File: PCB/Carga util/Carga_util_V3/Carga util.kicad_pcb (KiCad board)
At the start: 2 copper layers, 50 x 48.5 mm, 42 parts, among them J1 UART, J2 CONN, J3 DEBUG, J4 BG51, Q1 NMOS, Q2 NMOS, SW1 Reset, U1 LM1117DT-3.3, U2 ATtiny85-20S

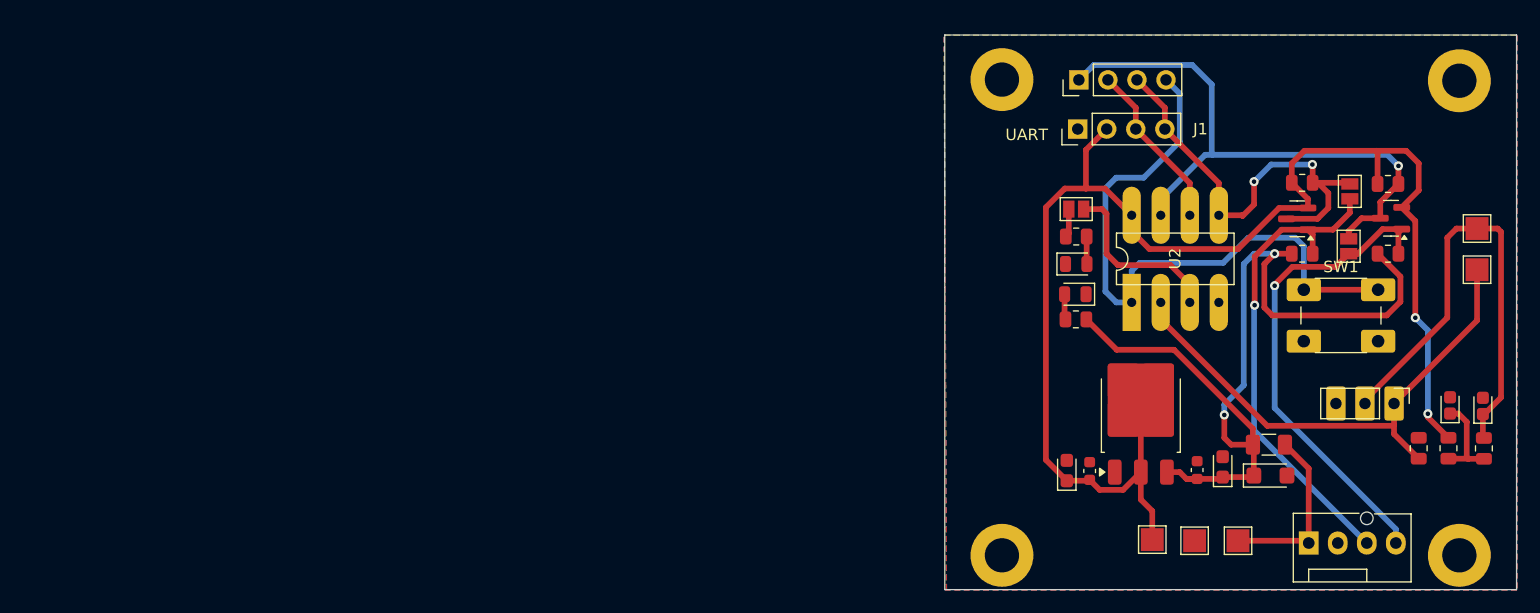
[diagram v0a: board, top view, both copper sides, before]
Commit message: update pcb para pocket
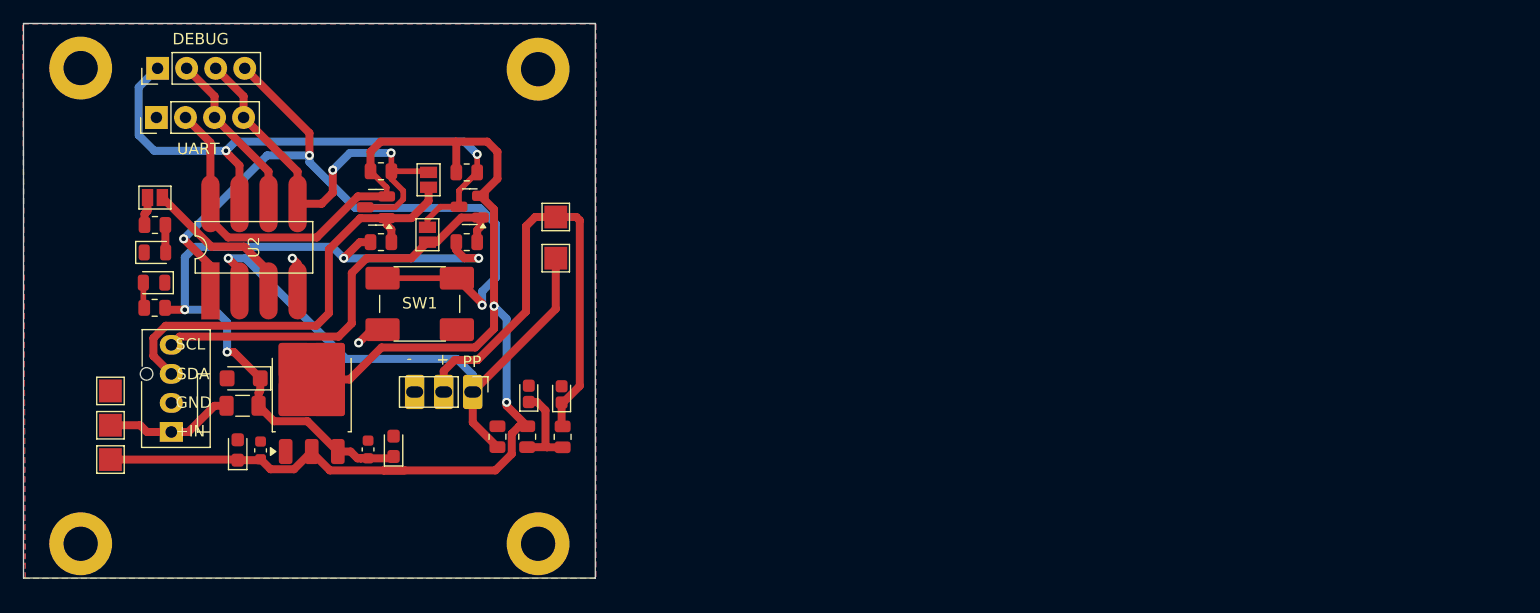
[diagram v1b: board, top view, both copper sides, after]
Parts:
- moved J2 99.9 mm to (132.3, 98.7), turned to 90 degrees
- moved IN 99.1 mm to (127.0, 98.1)
- moved GND 95.7 mm to (127.0, 95.1)
- moved +3.3V 91.4 mm to (127.0, 101.1)
- moved D1 90.2 mm to (138.7, 94.0), turned to 180 degrees
- moved F1 89.8 mm to (138.6, 96.4), turned to 180 degrees
- moved ? 80.6 mm to (124.4, 66.9)
- moved C5 80.6 mm to (163.6, 95.4)
- moved C6 80.6 mm to (166.4, 95.4)
- moved D2 80.6 mm to (130.8, 85.6)
- moved D3 80.6 mm to (130.9, 83.0)
- moved J1 80.6 mm to (131.0, 71.2)
- moved J3 80.6 mm to (131.1, 66.9)
- moved J4 80.6 mm to (158.7, 95.2)
- moved JP1 80.6 mm to (130.9, 78.2)
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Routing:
- net +3.7V: track 76.6 -> 65.7 mm, vias 2 -> 4
- net /SS: track 55.4 -> 66.0 mm, vias 0 -> 3
- net +3.3V: track 124.8 -> 135.2 mm
- net GND: track 0.00 -> 6.64 mm, vias 0 -> 2
- net /SCL_HV: track 42.7 -> 36.5 mm, vias 1 -> 0
- net /PP: track 46.2 -> 52.3 mm, vias 0 -> 1
- net /IN: track 15.7 -> 11.3 mm
- net /SDA_HV: track 42.6 -> 39.5 mm, vias 1 -> 0
- net Net-(JP1-B): track 15.6 -> 13.7 mm
- net /VDC_Filter: track 41.4 -> 42.6 mm
- net /SCK: track 52.4 -> 51.8 mm, vias 1 -> 2
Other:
- board text added: "+"
- board text added: "+IN"
- board text added: "-"
- board text added: "GND"
- board text added: "PP"
- board text added: "SCL"
- board text added: "SDA"

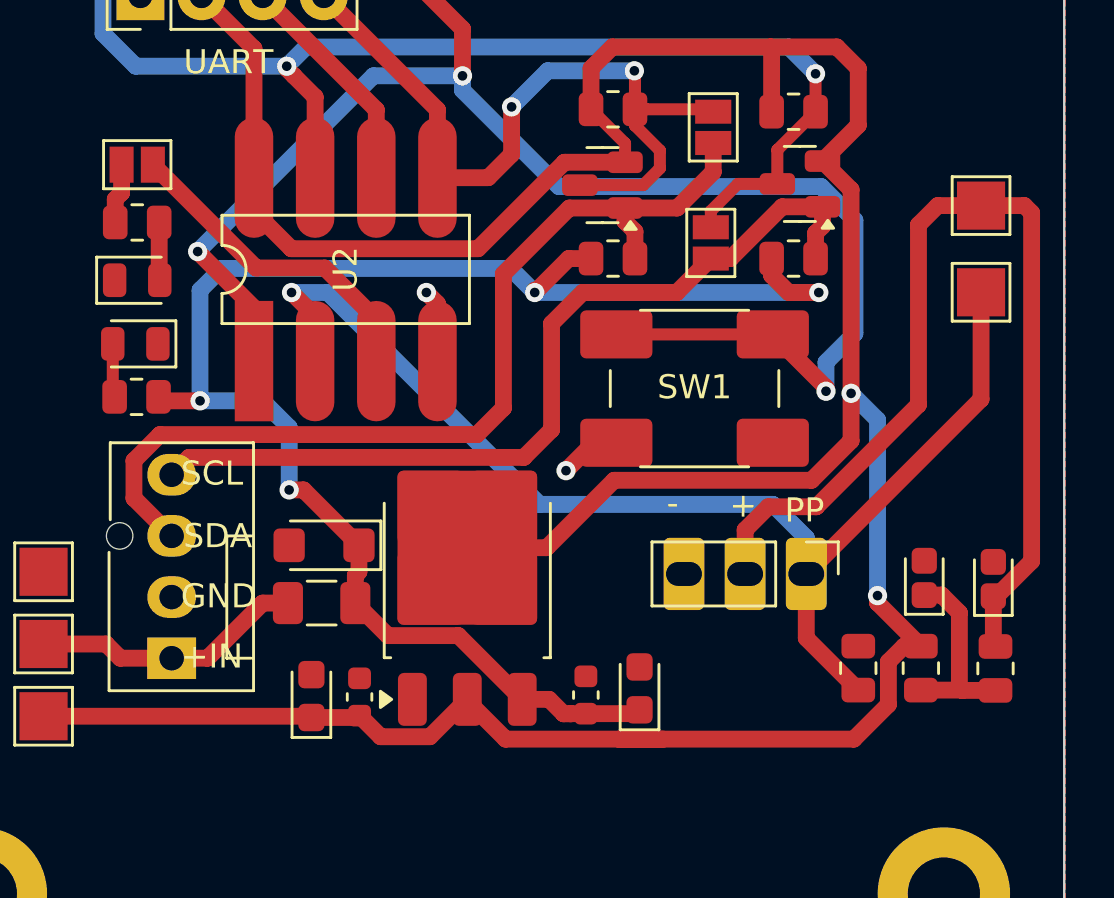
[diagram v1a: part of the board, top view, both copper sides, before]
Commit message: update 2 pcb pocket
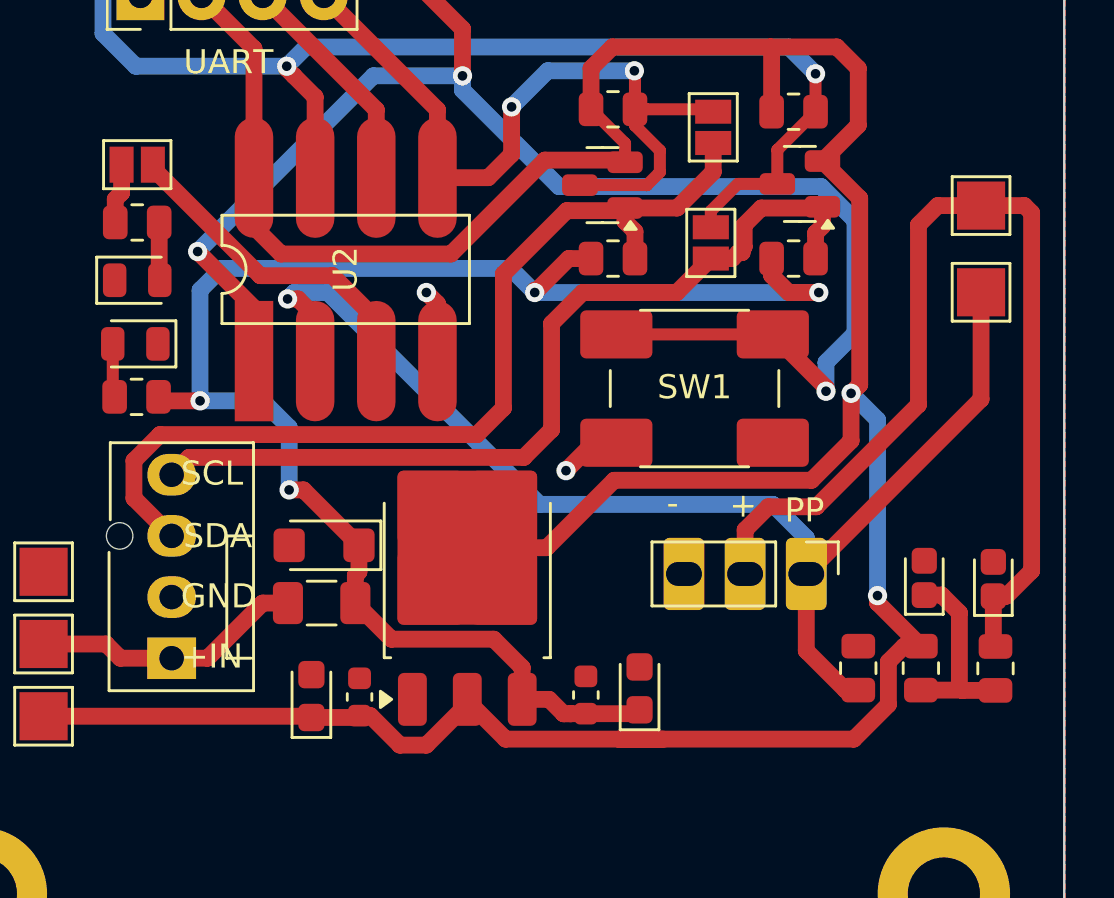
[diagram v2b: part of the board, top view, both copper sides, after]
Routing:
- net +3.3V: track 135.2 -> 136.6 mm
- net +3.7V: track 65.7 -> 66.5 mm
- net /SCL_HV: track 36.5 -> 37.2 mm
- net /PP: track 52.3 -> 52.9 mm
